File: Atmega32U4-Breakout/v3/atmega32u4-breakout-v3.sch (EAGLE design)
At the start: 54 parts, among them U1 ATMEGA32U4

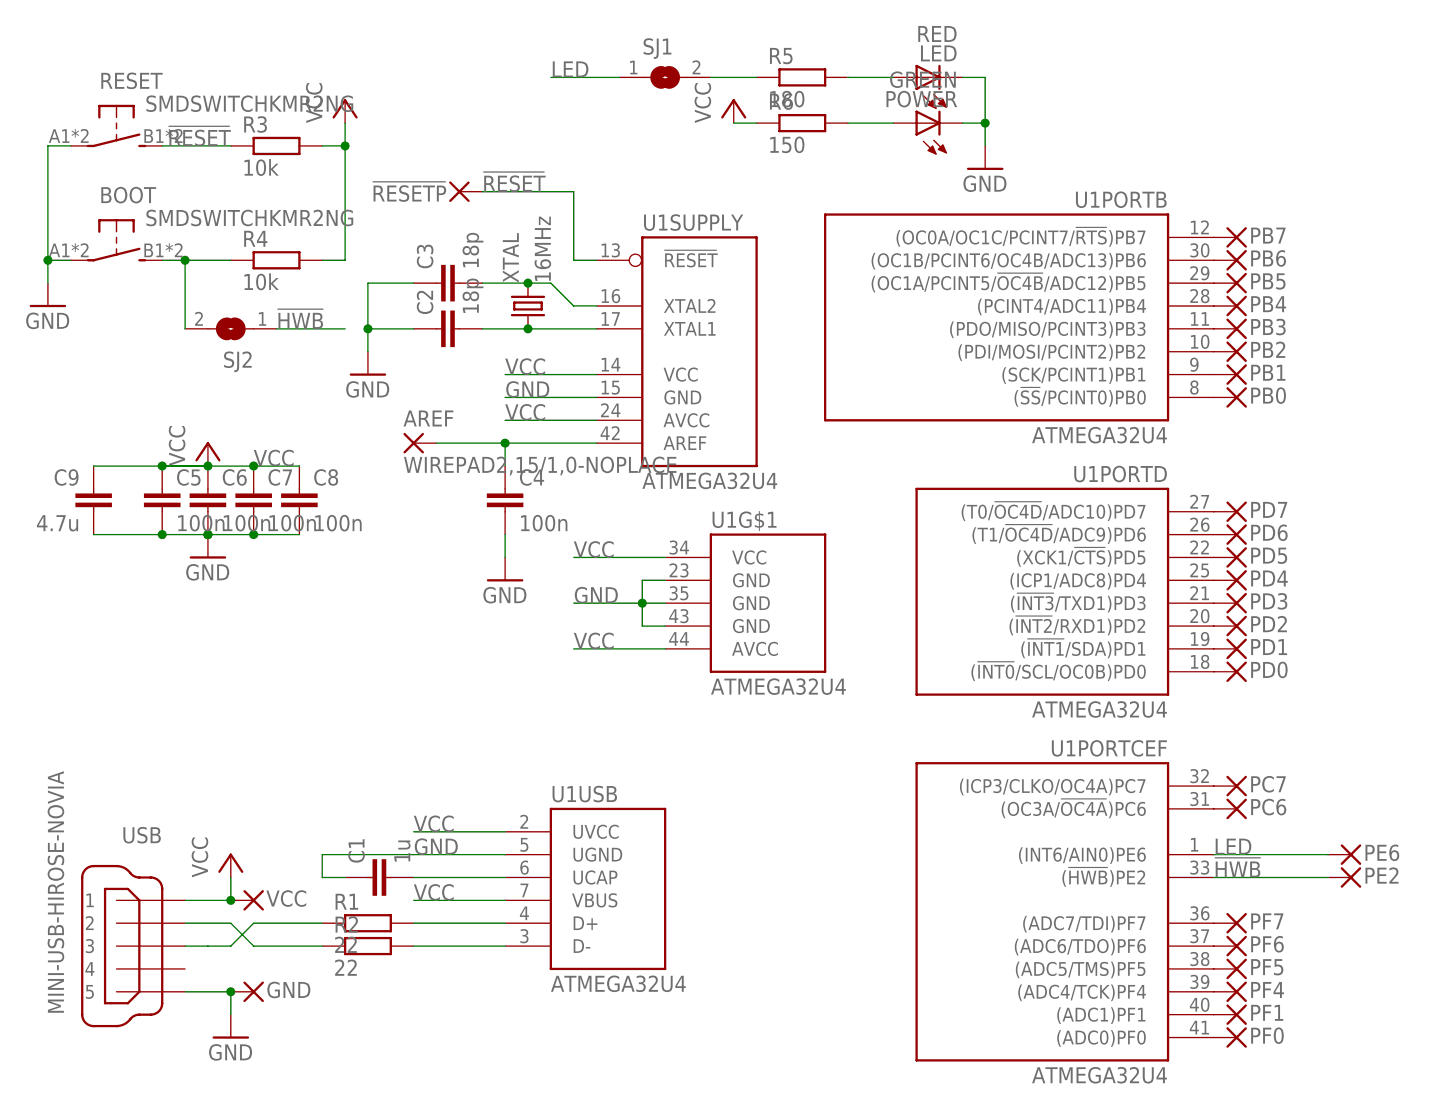
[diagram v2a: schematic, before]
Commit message: TinyMega v2 with optional 3V3 supply
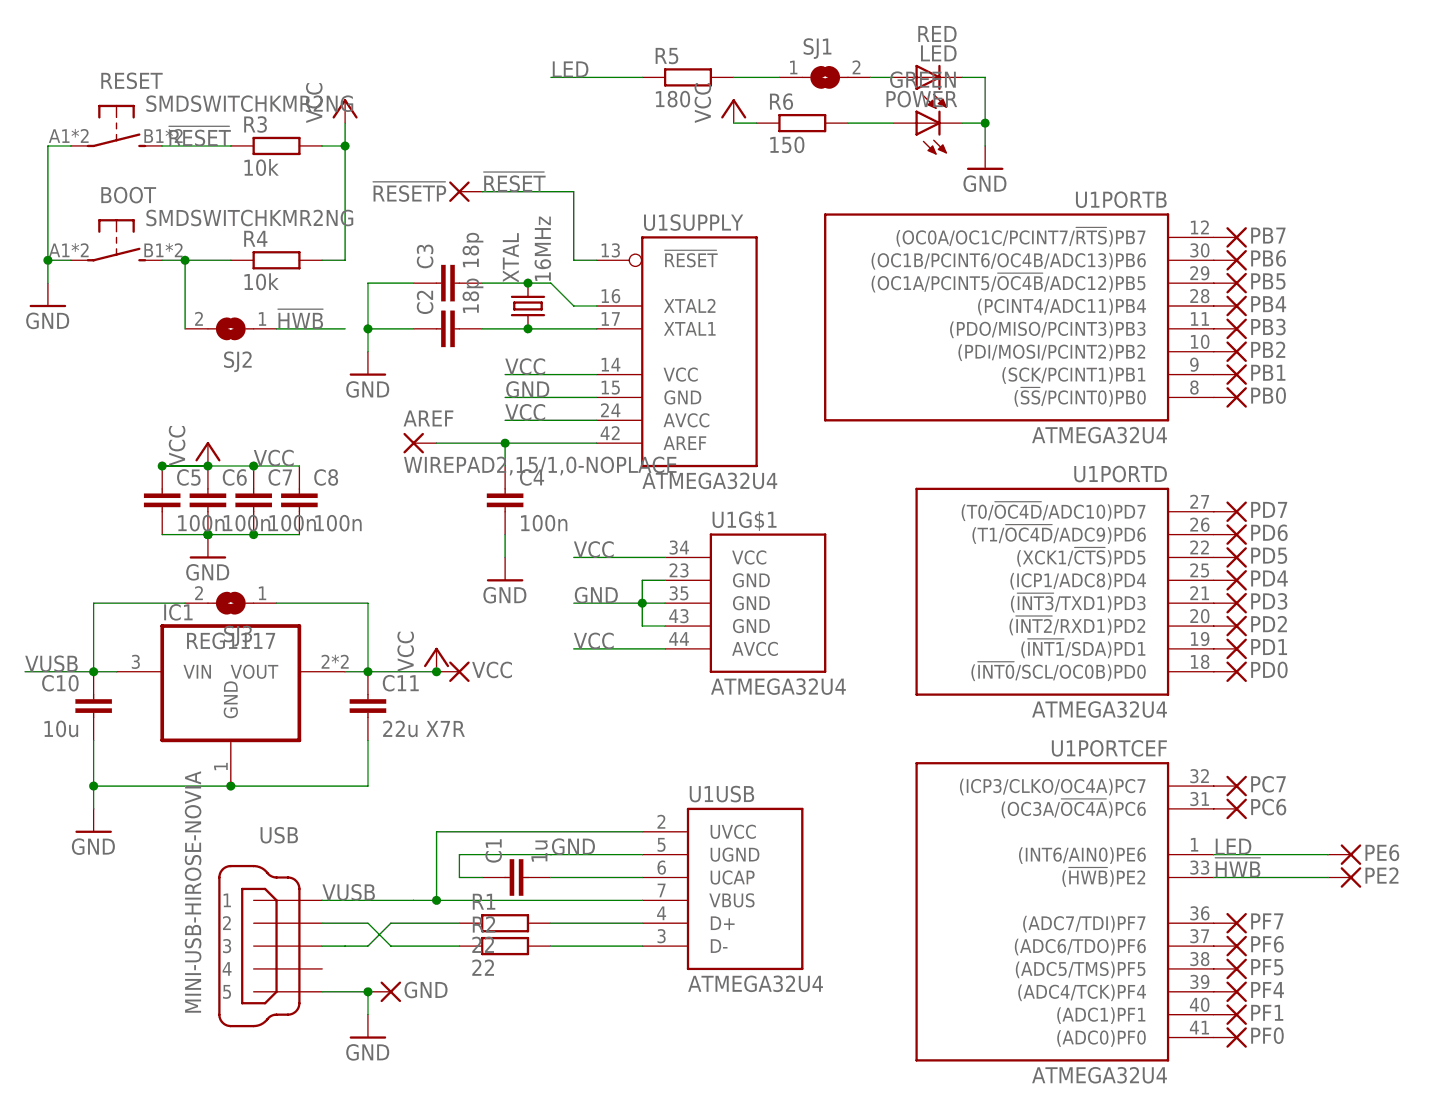
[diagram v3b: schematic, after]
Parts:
- removed C9: 4.7u, rcl:C-EUC0805K
- added C10: 10u, rcl:C-EUC0805K
- added C11: 22u X7R, rcl:C-EUC1206K
- added IC1: REG1117, burr-brown:REG1117
- added SJ3: (no value), jumper:SJ
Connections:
- new net VUSB: C10.1, IC1.VIN, SJ3.2, U1USB.UVCC, U1USB.VBUS, USB.1
- net GND: now also C10.2, C11.2, IC1.GND; no longer C9.2
- net LED: now also R5.1; no longer SJ1.1
- net N$11: now also SJ1.2; no longer R5.2
- net N$4: now also R5.2, SJ1.1; no longer R5.1, SJ1.2
- net VCC: now also C11.1, IC1.VOUT, SJ3.1; no longer C9.1, U1USB.UVCC, U1USB.VBUS, USB.1
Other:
- moved on the sheet: C1, GND, R1, R2, R5, SJ1, U1USB, USB, VCC
